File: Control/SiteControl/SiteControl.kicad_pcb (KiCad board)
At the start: 2 copper layers, 52.5 x 115.5 mm, 162 parts, among them J1 RJ50, J2 CONN_01X03, J3 IDC_16Pin_Polarized, J4 CONN_01X06, J5 IDC-10_Polarized, J6 CONN_01X02, J7 Molex Minifit-JR 4.2mm, Q1 BC817-40, Q2 SI2323DDS-T1-GE3, U1 Opto_H11L1M, U10 LMV611, U11 LM43602, U12 ICL3221, U13 Opto_H11L1M, U14 Opto_H11L1M, U15 12-Bit SPI ADC, U16 MCP7952, U17 74HCT125D,653, U18 SN74AUP1T87_Schmitt_XNOR, U2 Opto_H11L1M, U3 Opto_H11L1M, U4 Opto_H11L1M, U5 Opto_H11L1M, U6 PIC16LF1947, U7 SS_Relay_VO14642AT, U8 SS_Relay_VO14642AT, U9 LM43602, X1 CFS-20632768EZBB_32.768kHz, Y1 4MHz

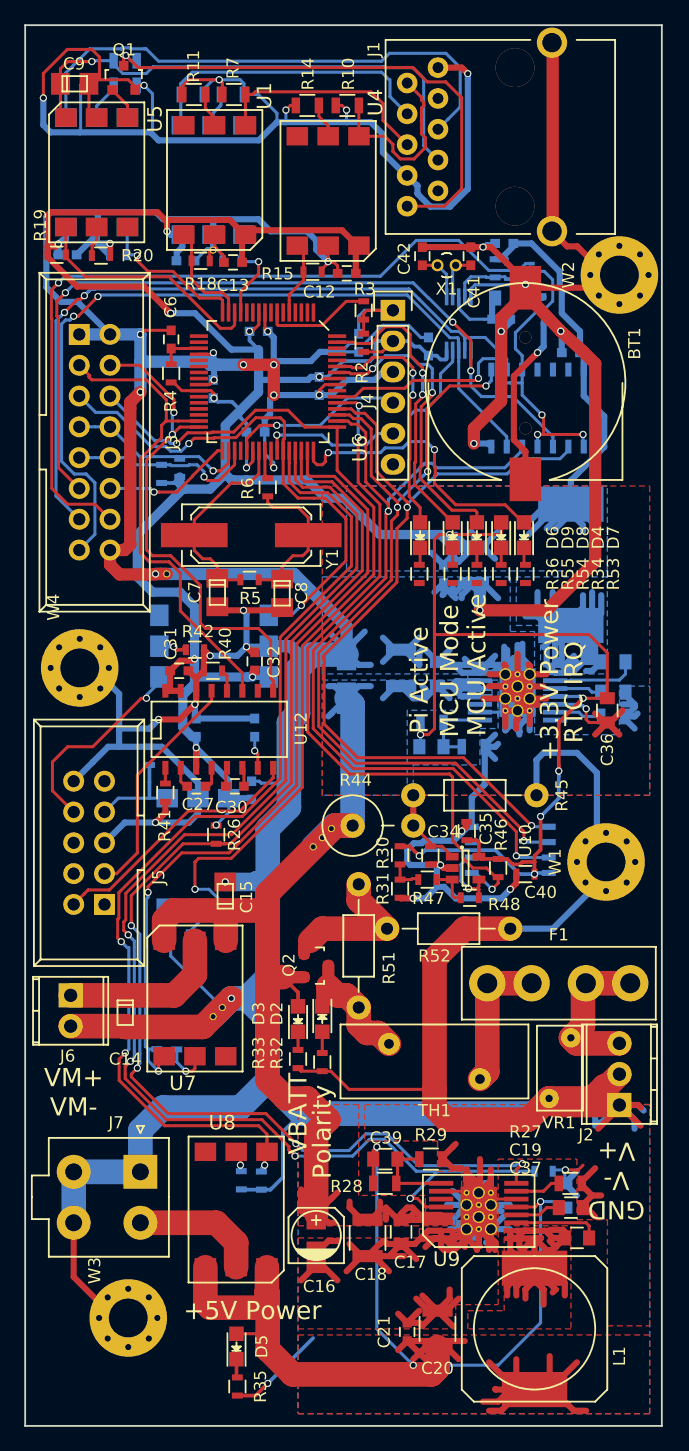
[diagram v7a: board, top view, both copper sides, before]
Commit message: [Added] More parts; [Completed] Site Control Rev B Layout
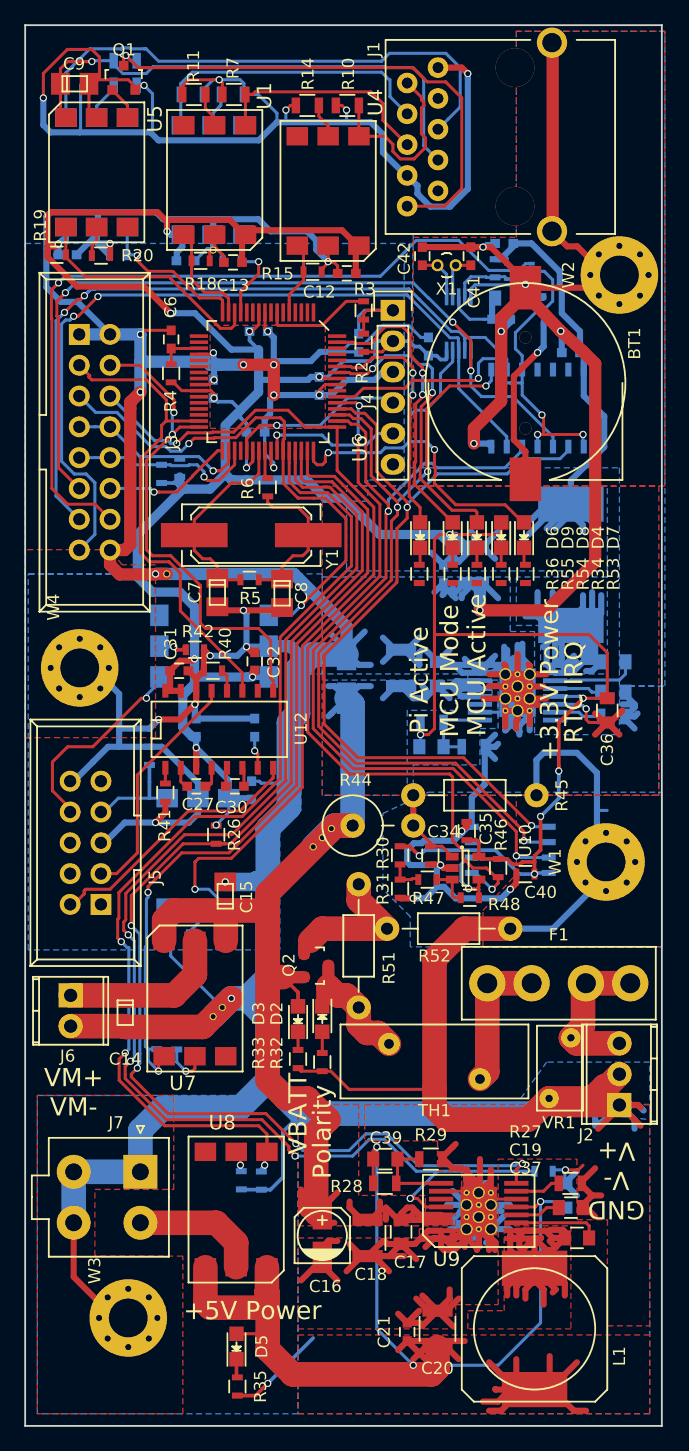
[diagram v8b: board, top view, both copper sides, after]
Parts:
- moved C16 0.50 mm to (173.9, 142.3)
- moved J5 0.29 mm to (155.6, 115.0)
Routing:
- net GND: track 942.6 -> 943.5 mm
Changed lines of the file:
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@@
     (thickness 1.6)
     (drawings 18)
-    (tracks 2367)
+    (tracks 2370)
     (zones 0)
     (modules 162)
@@
   (page A4)
   (layers
-    (0 F.Cu signal hide)
-    (31 B.Cu signal hide)
+    (0 F.Cu signal)
+    (31 B.Cu signal)
     (32 B.Adhes user)
     (33 F.Adhes user)
@@
   )
   (module Connect:IDC_Header_Straight_10pins (layer F.Cu)
-    (at 155.9 115 90)
+    (at 155.61 115 90)
     (descr "10 pins through hole IDC header")
     (tags "IDC header socket VASCH")
@@
   )
   (module Capacitors_SMD:c_elec_4x5.8 (layer F.Cu)
-    (at 173.36 142.30086 90)
+    (at 173.86 142.30086 90)
     (descr "SMT capacitor, aluminium electrolytic, 4x5.8")
     (attr smd)
@@
   (segment (start 178.419 66.011) (end 179.685 66.011) (width 0.25) (layer F.Cu) (net 1))
   (segment (start 177.272 67.94) (end 177.272 66.588) (width 0.25) (layer F.Cu) (net 1))
+  (segment (start 196.505999 107.25) (end 196.505999 104.145999) (width 0.508) (layer B.Cu) (net 2))
+  (segment (start 196.505999 110.745999) (end 196.505999 107.25) (width 0.508) (layer B.Cu) (net 2))
+  (segment (start 196.505999 107.25) (end 197.36 107.25) (width 0.25) (layer B.Cu) (net 2))
   (segment (start 188.11 60.5) (end 187.409252 60.5) (width 0.25) (layer B.Cu) (net 2))
   (segment (start 187.409252 60.5) (end 187.11 60.799252) (width 0.25) (layer B.Cu) (net 2))
@@
   (segment (start 196.505999 104.145999) (end 194.86 102.5) (width 0.508) (layer B.Cu) (net 2))
   (segment (start 197.26 111.5) (end 196.505999 110.745999) (width 0.508) (layer B.Cu) (net 2))
-  (segment (start 196.505999 110.745999) (end 196.505999 104.145999) (width 0.508) (layer B.Cu) (net 2))
   (segment (start 160.11 87.75) (end 161.037052 87.75) (width 1.016) (layer F.Cu) (net 2))
   (segment (start 156.36 85.78) (end 156.36 87.001314) (width 1.016) (layer F.Cu) (net 2))
@@
   (segment (start 182.774167 110.202147) (end 183.724167 110.202147) (width 0.25) (layer F.Cu) (net 70))
   (segment (start 183.724167 110.202147) (end 184.574167 111.052147) (width 0.25) (layer F.Cu) (net 70))
-  (segment (start 154.550601 113.809399) (end 154.223599 114.136401) (width 0.254) (layer F.Cu) (net 72))
-  (segment (start 156.300601 113.809399) (end 154.550601 113.809399) (width 0.254) (layer F.Cu) (net 72))
+  (segment (start 169.811 103.737) (end 169.811 104.5625) (width 0.254) (layer F.Cu) (net 72))
   (segment (start 167.075511 107.297989) (end 162.812011 107.297989) (width 0.254) (layer F.Cu) (net 72))
-  (segment (start 162.812011 107.297989) (end 156.300601 113.809399) (width 0.254) (layer F.Cu) (net 72))
-  (segment (start 154.223599 114.136401) (end 153.36 115) (width 0.254) (layer F.Cu) (net 72))
   (segment (start 169.811 104.5625) (end 167.075511 107.297989) (width 0.254) (layer F.Cu) (net 72))
-  (segment (start 169.811 103.737) (end 169.811 104.5625) (width 0.254) (layer F.Cu) (net 72))
+  (segment (start 162.812011 107.297989) (end 156.36 113.75) (width 0.254) (layer F.Cu) (net 72))
+  (segment (start 154.223599 113.886401) (end 154.223599 114.136401) (width 0.254) (layer F.Cu) (net 72))
+  (segment (start 156.36 113.75) (end 154.36 113.75) (width 0.254) (layer F.Cu) (net 72))
+  (segment (start 154.36 113.75) (end 154.223599 113.886401) (width 0.254) (layer F.Cu) (net 72))
+  (segment (start 154.223599 114.136401) (end 153.36 115) (width 0.254) (layer F.Cu) (net 72))
   (segment (start 164.731 97.387) (end 164.731 98.2125) (width 0.254) (layer F.Cu) (net 73))
   (segment (start 156.9 112.46) (end 155.9 112.46) (width 0.254) (layer F.Cu) (net 73))
@@
     (polygon
       (pts
-        (xy 191.36 98) (xy 191.36 101) (xy 198.36 101) (xy 198.36 97) (xy 200.86 97)
-        (xy 200.86 106) (xy 181.36 106) (xy 181.36 103.5) (xy 186.86 103.5) (xy 186.86 100.5)
+        (xy 191.36 98) (xy 191.36 101) (xy 198.36 101) (xy 198.36 97) (xy 201.61 97)
+        (xy 201.61 106) (xy 181.36 106) (xy 181.36 103.5) (xy 186.86 103.5) (xy 186.86 100.5)
         (xy 188.36 100.5) (xy 188.36 98)
       )
@@
     (polygon
       (pts
-        (xy 173.86 106) (xy 173.86 80.5) (xy 200.86 80.5) (xy 200.86 106)
+        (xy 173.86 106) (xy 173.86 80.5) (xy 201.61 80.5) (xy 201.61 106)
+      )
+    )
+  )
+  (zone (net 2) (net_name GND) (layer B.Cu) (hatch edge 0.508)
+    (connect_pads (clearance 0.254))
+    (min_thickness 0.254)
+    (fill yes (arc_segments 16) (thermal_gap 0.508) (thermal_bridge_width 0.508))
+    (polygon
+      (pts
+        (xy 201.86 118.5) (xy 181.11 118.5) (xy 181.11 116) (xy 178.86 113.75) (xy 178.86 108.5)
+        (xy 178.86 107.5) (xy 182.61 105.75) (xy 201.86 105.75)
+      )
+    )
+  )
+  (zone (net 2) (net_name GND) (layer B.Cu) (hatch edge 0.508)
+    (connect_pads (clearance 0.254))
+    (min_thickness 0.254)
+    (fill yes (arc_segments 16) (thermal_gap 0.508) (thermal_bridge_width 0.508))
+    (polygon
+      (pts
+        (xy 200.86 132.75) (xy 200.86 128) (xy 192.36 128) (xy 189.86 131.5)
+      )
+    )
+  )
+  (zone (net 2) (net_name GND) (layer B.Cu) (hatch edge 0.508)
+    (connect_pads (clearance 0.254))
+    (min_thickness 0.254)
+    (fill yes (arc_segments 16) (thermal_gap 0.508) (thermal_bridge_width 0.508))
+    (polygon
+      (pts
+        (xy 202.11 97) (xy 202.11 43) (xy 189.86 43) (xy 189.86 58.5) (xy 189.86 59.75)
+        (xy 181.36 59.75) (xy 181.11 79) (xy 198.36 79) (xy 198.36 97)
+      )
+    )
+  )
+  (zone (net 2) (net_name GND) (layer B.Cu) (hatch edge 0.508)
+    (connect_pads (clearance 0.254))
+    (min_thickness 0.254)
+    (fill yes (arc_segments 16) (thermal_gap 0.508) (thermal_bridge_width 0.508))
+    (polygon
+      (pts
+        (xy 171.86 157) (xy 150.36 157) (xy 150.36 130.75) (xy 171.86 130.75)
+      )
+    )
+  )
+  (zone (net 0) (net_name "") (layer B.Cu) (hatch edge 0.508)
+    (connect_pads (clearance 0.254))
+    (min_thickness 0.254)
+    (keepout (tracks not_allowed) (vias not_allowed) (copperpour not_allowed))
+    (fill (arc_segments 16) (thermal_gap 0.508) (thermal_bridge_width 0.508))
+    (polygon
+      (pts
+        (xy 155.11 138.5) (xy 155.11 144) (xy 163.11 144) (xy 163.11 138.5)
+      )
+    )
+  )
+  (zone (net 2) (net_name GND) (layer B.Cu) (hatch edge 0.508)
+    (connect_pads (clearance 0.254))
+    (min_thickness 0.254)
+    (fill yes (arc_segments 16) (thermal_gap 0.508) (thermal_bridge_width 0.508))
+    (polygon
+      (pts
+        (xy 170.36 118.75) (xy 149.61 118.75) (xy 149.61 87.75) (xy 173.86 87.75) (xy 173.86 96)
+        (xy 172.11 96) (xy 172.11 107.25) (xy 170.36 109)
+      )
+    )
+  )
+  (zone (net 2) (net_name GND) (layer B.Cu) (hatch edge 0.508)
+    (connect_pads (clearance 0.254))
+    (min_thickness 0.254)
+    (fill yes (arc_segments 16) (thermal_gap 0.508) (thermal_bridge_width 0.508))
+    (polygon
+      (pts
+        (xy 149.36 87.75) (xy 149.36 60.5) (xy 181.11 60.5) (xy 180.61 62.25) (xy 180.61 80)
+        (xy 177.61 80) (xy 177.61 81.75) (xy 174.11 81.75) (xy 172.11 80) (xy 165.36 80)
+        (xy 164.61 80.75) (xy 162.36 80.75) (xy 158.86 84.25) (xy 158.86 87.75)
+      )
+    )
+  )
+  (zone (net 2) (net_name GND) (layer F.Cu) (hatch edge 0.508)
+    (connect_pads (clearance 0.254))
+    (min_thickness 0.254)
+    (fill yes (arc_segments 16) (thermal_gap 0.508) (thermal_bridge_width 0.508))
+    (polygon
+      (pts
+        (xy 202.11 80.5) (xy 181.36 80.5) (xy 181.36 60) (xy 189.86 60) (xy 189.86 43)
+        (xy 202.11 43)
+      )
+    )
+  )
+  (zone (net 2) (net_name GND) (layer F.Cu) (hatch edge 0.508)
+    (connect_pads (clearance 0.254))
+    (min_thickness 0.254)
+    (fill yes (arc_segments 16) (thermal_gap 0.508) (thermal_bridge_width 0.508))
+    (polygon
+      (pts
+        (xy 164.61 75.75) (xy 174.11 75.75) (xy 174.11 67.25) (xy 164.61 67.25)
+      )
+    )
+  )
+  (zone (net 2) (net_name GND) (layer F.Cu) (hatch edge 0.508)
+    (connect_pads (clearance 0.254))
+    (min_thickness 0.254)
+    (fill yes (arc_segments 16) (thermal_gap 0.508) (thermal_bridge_width 0.508))
+    (polygon
+      (pts
+        (xy 150.36 157) (xy 162.36 157) (xy 162.36 144) (xy 155.11 144) (xy 155.11 138.5)
+        (xy 161.61 138.5) (xy 161.61 130.75) (xy 150.36 130.75)
+      )
+    )
+  )
+  (zone (net 2) (net_name GND) (layer F.Cu) (hatch edge 0.508)
+    (connect_pads (clearance 0.254))
+    (min_thickness 0.254)
+    (fill yes (arc_segments 16) (thermal_gap 0.508) (thermal_bridge_width 0.508))
+    (polygon
+      (pts
+        (xy 201.86 118.5) (xy 187.11 118.5) (xy 187.11 115.5) (xy 189.86 112.5) (xy 189.86 106)
+        (xy 201.86 106)
+      )
+    )
+  )
+  (zone (net 2) (net_name GND) (layer F.Cu) (hatch edge 0.508)
+    (connect_pads (clearance 0.254))
+    (min_thickness 0.254)
+    (fill yes (arc_segments 16) (thermal_gap 0.508) (thermal_bridge_width 0.508))
+    (polygon
+      (pts
+        (xy 149.36 101.25) (xy 160.11 101.25) (xy 160.11 87) (xy 157.36 87) (xy 156.36 85.75)
+        (xy 149.36 85.75)
       )
     )
